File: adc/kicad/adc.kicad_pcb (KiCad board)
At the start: 2 copper layers, 34.4 x 27.5 mm, 70 parts, among them J1 Conn_01x05_Pin, J2 Conn_01x06_Pin, J3 Conn_01x05_Pin, J4 Conn_01x03_Pin, U1 ESD5344D-TP, U2 ESD5344D-TP, U3 ADS1261B, U4 ESD5344D-TP, U5 TPS7A2050PDBVR, U6 TPS61252DSG, U7 XC6206P332MR

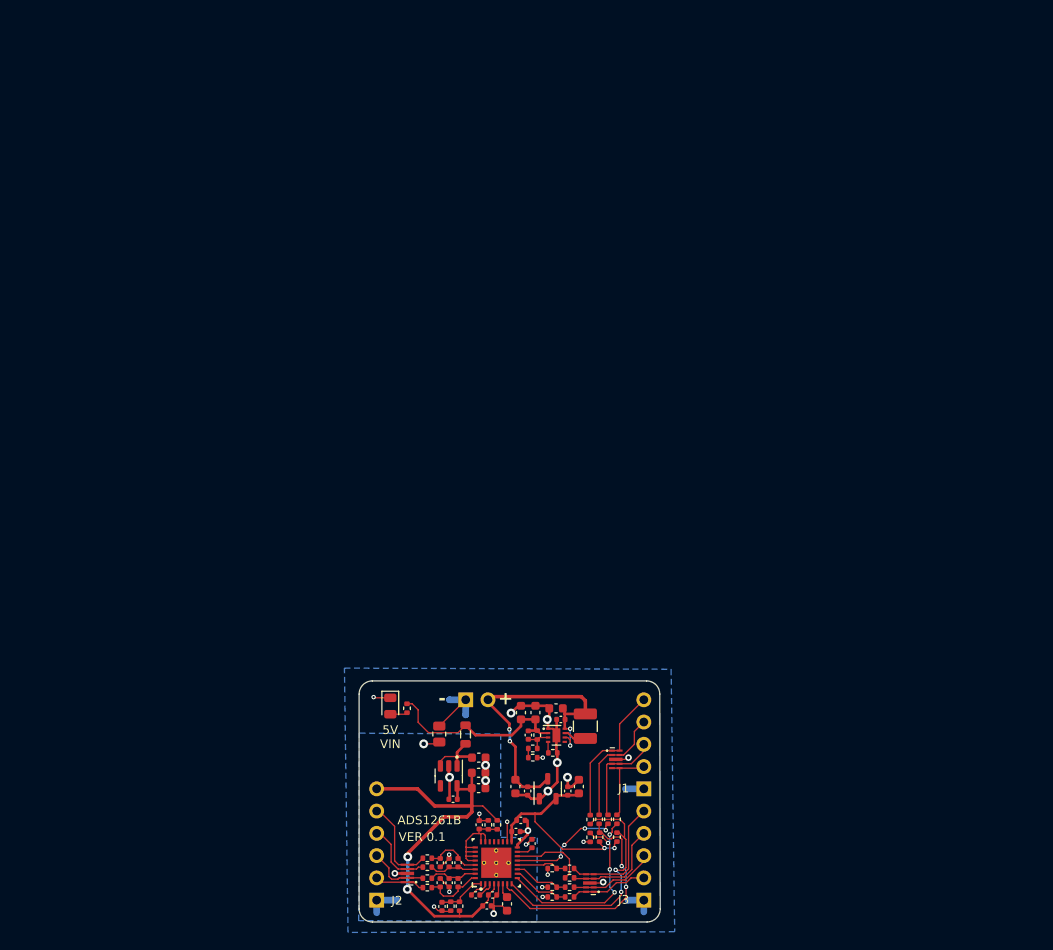
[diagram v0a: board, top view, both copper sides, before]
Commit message: Progressing on the ADC layout.
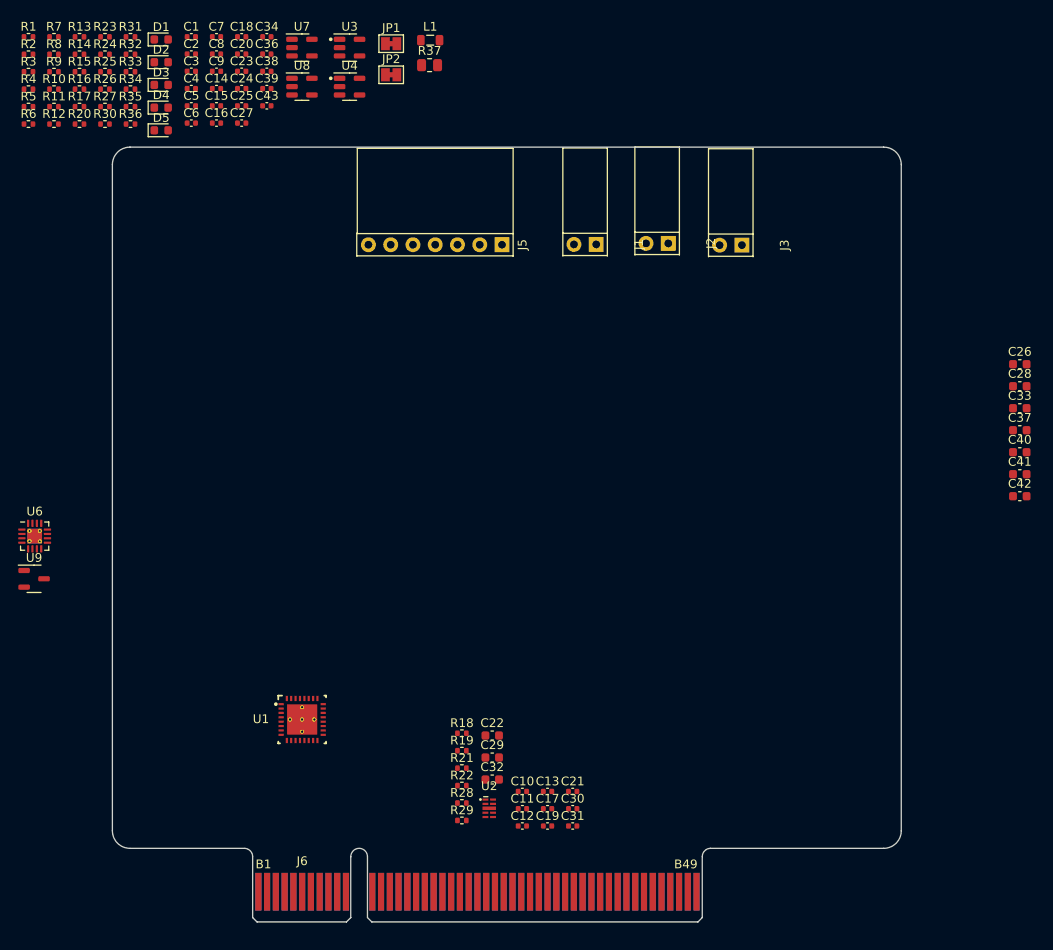
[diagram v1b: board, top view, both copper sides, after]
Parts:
- removed FB1: Ferrite Bead, Inductor_SMD:L_0805_2012Metric
- removed J4: Conn_01x03_Pin, adc:PinHeader_1x02_P2.54mm_Vertical
- removed U5: TPS7A2050PDBVR, adc:SOT-23-5
- added C29: 10u, Capacitor_SMD:C_0603_1608Metric, F.Cu at (15.2, -18.8)
- added C30: 100n, Capacitor_SMD:C_0402_1005Metric, F.Cu at (24.4, -12.9)
- added C31: 100n, Capacitor_SMD:C_0402_1005Metric, F.Cu at (24.4, -10.9)
- added C32: 10u, Capacitor_SMD:C_0603_1608Metric, F.Cu at (15.2, -16.2)
- added C33: 10u, Capacitor_SMD:C_0603_1608Metric, F.Cu at (75.4, -58.6)
- added C34: 100n, Capacitor_SMD:C_0402_1005Metric, F.Cu at (-10.5, -101.0)
- added C36: 100n, Capacitor_SMD:C_0402_1005Metric, F.Cu at (-10.5, -99.0)
- added C37: 10u, Capacitor_SMD:C_0603_1608Metric, F.Cu at (75.4, -56.1)
- added C38: 100n, Capacitor_SMD:C_0402_1005Metric, F.Cu at (-10.5, -97.0)
- added C39: 100n, Capacitor_SMD:C_0402_1005Metric, F.Cu at (-10.5, -95.1)
- added C40: 10u, Capacitor_SMD:C_0603_1608Metric, F.Cu at (75.4, -53.6)
- added C41: 10u, Capacitor_SMD:C_0603_1608Metric, F.Cu at (75.4, -51.1)
- added C42: 10u, Capacitor_SMD:C_0603_1608Metric, F.Cu at (75.4, -48.6)
- added C43: 100n, Capacitor_SMD:C_0402_1005Metric, F.Cu at (-10.5, -93.1)
- added D2: RED, LED_SMD:LED_0603_1608Metric, F.Cu at (-22.6, -98.1)
- added D3: RED, LED_SMD:LED_0603_1608Metric, F.Cu at (-22.6, -95.5)
- added D4: RED, LED_SMD:LED_0603_1608Metric, F.Cu at (-22.6, -92.9)
- added D5: RED, LED_SMD:LED_0603_1608Metric, F.Cu at (-22.6, -90.3)
- added J2: Conn_01x02_Pin, adc:connector_2pins_horizontal, F.Cu at (34.0, -77.4)
- added J6: pcie_98, common:PCIE_98_CARD, F.Cu at (0.00, 0.00)
- added JP1: SolderJumper_2_Bridged, Jumper:SolderJumper-2_P1.3mm_Bridged_Pad1.0x1.5mm, F.Cu at (3.66, -100.2)
- added JP2: SolderJumper_2_Bridged, Jumper:SolderJumper-2_P1.3mm_Bridged_Pad1.0x1.5mm, F.Cu at (3.66, -96.7)
- added R29: 51K, Resistor_SMD:R_0402_1005Metric, F.Cu at (11.7, -11.6)
- added R30: 1K 0.1% 10ppm, Resistor_SMD:R_0402_1005Metric, F.Cu at (-29.0, -91.0)
- added R31: 360K 0.1%, Resistor_SMD:R_0402_1005Metric, F.Cu at (-26.1, -101.0)
- added R32: 100K 0.1%, Resistor_SMD:R_0402_1005Metric, F.Cu at (-26.1, -99.0)
- added R33: 464K 0.1%, Resistor_SMD:R_0402_1005Metric, F.Cu at (-26.1, -97.0)
- added R34: 1K, Resistor_SMD:R_0402_1005Metric, F.Cu at (-26.1, -95.0)
- added R35: 1K 0.1% 10ppm, Resistor_SMD:R_0402_1005Metric, F.Cu at (-26.1, -93.0)
- added R36: 1K 0.1% 10ppm, Resistor_SMD:R_0402_1005Metric, F.Cu at (-26.1, -91.0)
- added R37: 0R, Resistor_SMD:R_0805_2012Metric, F.Cu at (8.04, -97.8)
- added U8: ADP7182AUJZ-2.5, Package_TO_SOT_SMD:TSOT-23-5, F.Cu at (-6.52, -95.3)
- added U9: XC6206P332MR, Package_TO_SOT_SMD:SOT-23-3, F.Cu at (-37.1, -39.1)
- C1, C5: value 1u -> 2u2
- C10: value 1n -> 1u
- C11: value 10n -> 1u
- C12: value 4n7 -> 100n
- C13, C8: value 1n -> 100n
- C14: value 1u -> 22n
- C15, C19: value 10u -> 220n; footprint Capacitor_SMD:C_0603_1608Metric -> Capacitor_SMD:C_0402_1005Metric
- C16: value 100pf -> 22n
- C17: value 10u -> 4n7; footprint Capacitor_SMD:C_0603_1608Metric -> Capacitor_SMD:C_0402_1005Metric
- C18: value 10u -> 22n; footprint Capacitor_SMD:C_0603_1608Metric -> Capacitor_SMD:C_0402_1005Metric
- C2, C9: value 1u -> 100n
- C20: value 100n -> 22n
- C21: value 10u -> 1u; footprint Capacitor_SMD:C_0603_1608Metric -> Capacitor_SMD:C_0402_1005Metric
- C22, C26: value 100n -> 10u; footprint Capacitor_SMD:C_0402_1005Metric -> Capacitor_SMD:C_0603_1608Metric
- C23, C24, C25: value 10u -> 100n; footprint Capacitor_SMD:C_0603_1608Metric -> Capacitor_SMD:C_0402_1005Metric
- C6: value 1n -> 2u2
- C7: value 10n -> 100n
- D1: footprint LED_SMD:LED_0805_2012Metric -> LED_SMD:LED_0603_1608Metric
- J1, J3: value Conn_01x05_Pin -> Conn_01x02_Pin; footprint adc:PinHeader_1x05_P2.54mm_Vertical -> adc:connector_2pins_horizontal
- J5: renamed from J2; value Conn_01x06_Pin -> Conn_01x07_Pin; footprint adc:PinHeader_1x06_P2.54mm_Vertical -> adc:connector_7pins_horizontal
- L1: value 1uH -> 2u2H; footprint Inductor_SMD:L_1210_3225Metric -> Inductor_SMD:L_0805_2012Metric
- R1, R13, R2, R7: value 51K -> 1K 0.1% 10ppm
- R10: value 100R -> 470R
- R11, R9: value 47R -> 470R
- R12, R17, R8: value 47R -> 1K 0.1% 10ppm
- R14, R3: value 100R -> 1K 0.1% 10ppm
- R15, R16: value 47R -> 51K
- R19: value 100R -> 47R
- R20: value 51K -> 1K
- R21, R22: value 51K -> 47R
- R23: value 510K -> 5K1
- R25: value 120K -> 5K1
- R26: value 20K -> 5K1
- R27: value 0R -> 5K1; footprint Resistor_SMD:R_0805_2012Metric -> Resistor_SMD:R_0402_1005Metric
- R28: value 22K -> 51K
- R4, R5, R6: value 51K -> 470R
- U1: value ESD5344D-TP -> ADS1261B; footprint common:Diodes_UDFN-10_1.0x2.5mm_P0.5mm -> adc:RHB0032E
- U3: value ADS1261B -> TPS7A2050PDBVR; footprint adc:RHB0032E -> adc:SOT-23-5
- U4: value ESD5344D-TP -> TPS7A2025PDBVR; footprint common:Diodes_UDFN-10_1.0x2.5mm_P0.5mm -> adc:SOT-23-5
- U6: value TPS61252DSG -> TPS65135; footprint adc:WSON-8-1EP_2x2mm_P0.5mm_EP0.9x1.6mm -> Package_DFN_QFN:WQFN-16-1EP_3x3mm_P0.5mm_EP1.68x1.68mm_ThermalVias
- U7: value XC6206P332MR -> ADP7182AUJZ-5.0; footprint Package_TO_SOT_SMD:SOT-23-3 -> Package_TO_SOT_SMD:TSOT-23-5
- moved R1 110.7 mm to (-37.7, -101.0), turned to 0 degrees
- moved R2 108.5 mm to (-37.7, -99.0), turned to 0 degrees
- moved R13 108.3 mm to (-31.9, -101.0), turned to 0 degrees
- moved R5 107.0 mm to (-37.7, -93.0), turned to 0 degrees
- moved R15 106.7 mm to (-31.9, -97.0), turned to 0 degrees
- moved R8 106.6 mm to (-34.8, -99.0), turned to 0 degrees
- moved R16 105.9 mm to (-31.9, -95.0), turned to 0 degrees
- moved R9 105.6 mm to (-34.8, -97.0), turned to 0 degrees
- moved R17 105.1 mm to (-31.9, -93.0), turned to 0 degrees
- moved C1 104.7 mm to (-19.1, -101.0), turned to 0 degrees
- moved R6 104.2 mm to (-37.7, -91.0), turned to 0 degrees
- moved R20 103.4 mm to (-31.9, -91.0)
- moved R11 103.0 mm to (-34.8, -93.0), turned to 0 degrees
- moved R7 102.7 mm to (-34.8, -101.0), turned to 0 degrees
- moved R12 102.1 mm to (-34.8, -91.0), turned to 0 degrees
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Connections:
- C1 pad 1: GNDA -> /AIN6
- C1 pad 2: +5VA -> /AIN7
- C10 pad 1: /AIN1 -> GNDA
- C10 pad 2: GNDA -> /+2V5A
- C11 pad 1: /AIN1 -> /+3V3D
- C11 pad 2: /AIN0 -> GNDD
- C12 pad 1: Net-(U3-CAPN) -> GNDA
- C12 pad 2: Net-(U3-CAPP) -> /+2V5A
- C13 pad 1: GNDA -> /+3V3D
- C13 pad 2: /AIN0 -> GNDD
- C14 pad 1: Net-(U3-BYPASS) -> /AIN2
- C15 pad 1: Net-(U3-REFOUT) -> /AIN0
- C15 pad 2: GNDA -> /AIN1
- C16 pad 1: Net-(U6-FB) -> GNDA
- C16 pad 2: Net-(U6-VOUT) -> /AIN1
- C17 pad 1: GNDD -> Net-(U1-CAPN)
- C17 pad 2: Net-(J4-Pin_2) -> Net-(U1-CAPP)
- C18 pad 1: GNDD -> /AIN0
- C18 pad 2: Net-(U6-VOUT) -> GNDA
- C19 pad 1: GNDD -> /AIN2
- C19 pad 2: Net-(U6-VOUT) -> /AIN3
- C2 pad 1: +3V3 -> GNDA
- C2 pad 2: GNDD -> /AIN6
- C20 pad 1: GNDD -> GNDA
- C20 pad 2: Net-(J4-Pin_2) -> /AIN3
- C21 pad 1: GNDA -> Net-(U1-BYPASS)
- C21 pad 2: Net-(U5-EN) -> GNDA
- C22 pad 1: GNDA -> Net-(U1-REFOUT)
- C22 pad 2: +5VA -> GNDA
- C23 pad 2: +5VA -> /+5V7
- C24 pad 2: +5VA -> /+5VA
- C25 pad 1: GNDD -> GNDA
- C25 pad 2: Net-(J4-Pin_2) -> /+5VA
- C26 pad 1: GNDD -> GNDA
- C26 pad 2: Net-(J4-Pin_2) -> /+5VA
- C27 pad 1: GNDD -> GNDA
- C27 pad 2: +3V3 -> /+2V5A
- C28 pad 1: GNDD -> GNDA
- C28 pad 2: +3V3 -> /+2V5A
- C3 pad 2: +5VA -> /AIN4
- C4 pad 1: +3V3 -> /AIN7
- C4 pad 2: GNDD -> GNDA
- C5 pad 1: GNDA -> /AIN8
- C5 pad 2: Net-(U3-AINCOM) -> /AIN9
- C6 pad 1: /AIN3 -> /AIN4
- C6 pad 2: GNDA -> /AIN5
- C7 pad 1: /AIN3 -> GNDA
- C7 pad 2: /AIN2 -> /AIN8
- C8 pad 1: GNDA -> /AIN9
- C8 pad 2: /AIN2 -> GNDA
- C9 pad 1: GNDA -> /AIN5
- C9 pad 2: Net-(U3-AIN4) -> GNDA
- D1 pad 1: GNDD -> GNDA
- J1 pad 1: GNDD -> Net-(J1-Pin_1)
- J3 pad 1: GNDD -> Net-(J3-Pin_1)
- J5 pad 1: GNDA -> /-5VA
- J5 pad 2: Net-(J2-Pin_2) -> Net-(J5-Pin_2)
- J5 pad 3: Net-(J2-Pin_3) -> Net-(J5-Pin_3)
- J5 pad 4: Net-(J2-Pin_4) -> GNDA
- J5 pad 5: Net-(J2-Pin_5) -> Net-(J5-Pin_5)
- J5 pad 6: +5VA -> Net-(J5-Pin_6)
- L1 pad 1: Net-(J4-Pin_2) -> Net-(L1-Pad1)
- L1 pad 2: Net-(U6-SW) -> Net-(L1-Pad2)
- R1 pad 1: Net-(U3-AINCOM) -> Net-(J1-Pin_2)
- R1 pad 2: +5VA -> /+2V5A
- R10 pad 1: Net-(J2-Pin_4) -> Net-(J2-Pin_2)
- R10 pad 2: /AIN2 -> /AIN8
- R11 pad 1: Net-(J1-Pin_3) -> Net-(J2-Pin_1)
- R11 pad 2: Net-(U3-DRDY_N) -> /AIN9
- R12 pad 1: Net-(J1-Pin_2) -> /-2V5A
- R12 pad 2: Net-(U3-START) -> Net-(J3-Pin_1)
- R13 pad 1: GNDD -> /AIN0
- R13 pad 2: Net-(U3-START) -> Net-(R13-Pad2)
- R14 pad 1: Net-(J2-Pin_3) -> Net-(R14-Pad1)
- R14 pad 2: /AIN1 -> /AIN0
- R15 pad 1: Net-(J3-Pin_5) -> Net-(U1-MISO)
- R15 pad 2: Net-(U3-DIN) -> /+3V3D
- R16 pad 1: Net-(J3-Pin_4) -> Net-(U1-CS_N)
- R16 pad 2: Net-(U3-DOUT_DRDY_N) -> /+3V3D
- R17 pad 1: Net-(J3-Pin_3) -> Net-(R13-Pad2)
- R17 pad 2: Net-(U3-SCLK) -> Net-(J5-Pin_6)
- R18 pad 1: Net-(J3-Pin_2) -> /PA7
- R18 pad 2: Net-(U3-CS_N) -> Net-(U1-MOSI)
- R19 pad 1: Net-(J2-Pin_2) -> /PA6
- R19 pad 2: /AIN0 -> Net-(U1-MISO)
- R2 pad 1: GNDA -> /-2V5A
- R2 pad 2: Net-(U3-AINCOM) -> Net-(J1-Pin_1)
- R20 pad 1: GNDD -> Net-(J5-Pin_3)
- R20 pad 2: Net-(U3-CS_N) -> /AIN3
- R21 pad 1: GNDD -> /PA5
- R21 pad 2: Net-(U3-SCLK) -> Net-(U1-SCLK)
- R22 pad 1: GNDD -> /PB14
- R22 pad 2: Net-(U3-DIN) -> Net-(U1-CS_N)
- R23 pad 1: Net-(U6-VOUT) -> /+5VA
- R23 pad 2: Net-(U6-FB) -> Net-(D1-A)
- R24 pad 1: Net-(U6-VOUT) -> /-5VA
- R24 pad 2: Net-(D1-A) -> Net-(D2-A)
- R25 pad 1: Net-(R25-Pad1) -> /+2V5A
- R25 pad 2: Net-(U6-FB) -> Net-(D3-A)
- R26 pad 1: Net-(U6-ILIM) -> /-2V5A
- R26 pad 2: GNDD -> Net-(D4-A)
- R27 pad 1: GNDD -> /+3V3D
- R27 pad 2: GNDA -> Net-(D5-A)
- R28 pad 2: Net-(R25-Pad1) -> Net-(U1-MOSI)
- R3 pad 1: Net-(J2-Pin_5) -> Net-(J3-Pin_2)
- R3 pad 2: /AIN3 -> /+2V5A
- R4 pad 1: Net-(U3-AIN4) -> Net-(J1-Pin_2)
- R4 pad 2: +5VA -> /AIN6
- R5 pad 1: Net-(U3-RESET_N) -> Net-(J1-Pin_1)
- R5 pad 2: +3V3 -> /AIN7
- R6 pad 1: Net-(U3-PWDN_N) -> Net-(J3-Pin_2)
- R6 pad 2: +3V3 -> /AIN4
- R7 pad 1: GNDA -> Net-(J2-Pin_2)
- R7 pad 2: Net-(U3-AIN4) -> /+2V5A
- R8 pad 1: Net-(J1-Pin_5) -> /-2V5A
- R8 pad 2: Net-(U3-RESET_N) -> Net-(J2-Pin_1)
- R9 pad 1: Net-(J1-Pin_4) -> Net-(J3-Pin_1)
- R9 pad 2: Net-(U3-PWDN_N) -> /AIN5
- U1 pad 1: Net-(J1-Pin_5) -> GNDA
- U1 pad 2: Net-(J1-Pin_4) -> Net-(U1-CAPP)
- U1 pad 3: GNDD -> Net-(U1-CAPN)
- U1 pad 4: Net-(J1-Pin_3) -> /+2V5A
- U1 pad 5: Net-(J1-Pin_2) -> /-2V5A
- U2 pad 1: Net-(J2-Pin_2) -> /PB14
- U2 pad 2: Net-(J2-Pin_3) -> /PA5
- U2 pad 3: GNDA -> GNDD
- U2 pad 4: Net-(J2-Pin_4) -> /PA6
- U2 pad 5: Net-(J2-Pin_5) -> /PA7
- U3 pad 1: Net-(U3-AINCOM) -> /+5V7
- U3 pad 2: Net-(U3-CAPP) -> GNDA
- U3 pad 3: Net-(U3-CAPN) -> /+5V7
- U3 pad 4: +5VA -> unconnected-(U3-NC-Pad4)
- U3 pad 5: GNDA -> /+5VA
- U4 pad 1: Net-(J3-Pin_2) -> /+5VA
- U4 pad 2: Net-(J3-Pin_3) -> GNDA
- U4 pad 3: GNDD -> /+5VA
- U4 pad 4: Net-(J3-Pin_4) -> unconnected-(U4-NC-Pad4)
- U4 pad 5: Net-(J3-Pin_5) -> /+2V5A
- U6 pad 1: GNDD -> +5VD
- U6 pad 2: Net-(U6-VOUT) -> /-5V7
- U6 pad 3: Net-(U6-FB) -> /-5V7
- U6 pad 4: Net-(U6-ILIM) -> Net-(U6-VAUX)
- U6 pad 5: unconnected-(U6-PG-Pad5) -> GNDA
- U6 pad 6: Net-(J4-Pin_2) -> Net-(U6-FBG)
- U6 pad 7: Net-(U6-SW) -> Net-(U6-FB)
- U6 pad 8: Net-(J4-Pin_2) -> +5VD
- U6 pad 9: GNDD -> /+5V7
- U7 pad 1: GNDD -> GNDA
- U7 pad 2: +3V3 -> /-5V7
- U7 pad 3: Net-(J4-Pin_2) -> /-5V7
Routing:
- net GNDD: track 53.4 -> 0.00 mm, vias 15 -> 0
- net +5VA: track 50.2 -> 0.00 mm, vias 2 -> 0
- net Net-(J4-Pin_2): track 37.6 -> 0.00 mm, vias 4 -> 0
- net Net-(U3-RESET_N): track 29.0 -> 0.00 mm, vias 2 -> 0
- net Net-(U3-PWDN_N): track 26.4 -> 0.00 mm, vias 2 -> 0
- net GNDA: track 24.8 -> 0.00 mm, vias 11 -> 0
- net +3V3: track 24.1 -> 0.00 mm, vias 2 -> 0
- net Net-(U3-START): track 23.9 -> 0.00 mm, vias 4 -> 0
- net Net-(U6-VOUT): track 22.6 -> 0.00 mm
- net Net-(J1-Pin_5): track 16.8 -> 0.00 mm
- net Net-(J1-Pin_4): track 14.1 -> 0.00 mm
- net Net-(J3-Pin_5): track 14.0 -> 0.00 mm
- net Net-(U3-AIN4): track 13.2 -> 0.00 mm
- net Net-(U3-DRDY_N): track 13.1 -> 0.00 mm, vias 4 -> 0
- net Net-(J3-Pin_4): track 11.8 -> 0.00 mm
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- removed copper zone on B.Cu, net GNDA
- removed copper zone on B.Cu, net GNDD
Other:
- board size 34.4 x 27.5 mm -> 90 x 88.4 mm
- board text removed: "+"
- board text removed: "-"
- board text removed: "5V VIN"
- board text removed: "ADS1261B"
- board text removed: "VER 0.1"

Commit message: More progress with the ADC layout.
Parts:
- moved C37 97.2 mm to (-20.2, -38.4), turned to 90 degrees
- moved C40 96.1 mm to (-20.3, -44.8), turned to 90 degrees
- moved R10 93.6 mm to (56.1, -72.8)
- moved R11 93.6 mm to (56.1, -70.8)
- moved R7 91.8 mm to (52.9, -74.0)
- moved R8 91.8 mm to (52.9, -72.0)
- moved C41 91.1 mm to (-12.7, -27.6)
- moved C26 89.1 mm to (-10.1, -38.4), turned to 90 degrees
- moved C42 88.8 mm to (-11.5, -30.0), turned to 90 degrees
- moved C33 87.2 mm to (-5.75, -26.5), turned to 90 degrees
- moved C28 86.8 mm to (-10.2, -46.3), turned to 90 degrees
- moved R15 86.0 mm to (33.4, -41.1)
- moved R2 85.7 mm to (43.5, -71.8), turned to 90 degrees
- moved R5 85.7 mm to (44.5, -69.2)
- moved R16 85.1 mm to (32.4, -39.3)
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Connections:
- U2 pad 2: /PA5 -> /PA6
- U2 pad 4: /PA6 -> /PA7
- U2 pad 5: /PA7 -> /PA5
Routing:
- net GNDA: track 0.00 -> 98.4 mm, vias 0 -> 15
- net +5VD: track 0.00 -> 94.7 mm
- net /-5VA: track 0.00 -> 89.6 mm
- net GNDD: track 0.00 -> 88.5 mm, vias 0 -> 3
- net /+5VA: track 0.00 -> 68.6 mm
- net /-2V5A: track 0.00 -> 25.5 mm, vias 0 -> 2
- net /-5V7: track 0.00 -> 20.5 mm, vias 0 -> 2
- net /PB14: track 0.00 -> 19.7 mm
- net /PA7: track 0.00 -> 17.3 mm, vias 0 -> 1
- net /PA5: track 0.00 -> 17.1 mm
- net /PA6: track 0.00 -> 14.3 mm
- net (no net): track 0.00 -> 14.1 mm
- net /+2V5A: track 0.00 -> 13.5 mm
- net /AIN1: track 0.00 -> 12.5 mm, vias 0 -> 2
- net /+5V7: track 0.00 -> 8.38 mm
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
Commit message: Initial topological routing of the ADC board completed.
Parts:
- added C35: 1u, Capacitor_SMD:C_0402_1005Metric, F.Cu at (16.6, -49.3)
- added C44: 100n, Capacitor_SMD:C_0402_1005Metric, F.Cu at (18.1, -49.7)
- added C45: 1u, Capacitor_SMD:C_0402_1005Metric, F.Cu at (23.0, -74.4)
- added C46: 1u, Capacitor_SMD:C_0402_1005Metric, F.Cu at (5.05, -74.2)
- added C47: 10u, Capacitor_SMD:C_0603_1608Metric, F.Cu at (2.04, -39.7)
- added C48: 10u, Capacitor_SMD:C_0603_1608Metric, F.Cu at (2.04, -37.2)
- moved R22 15.9 mm to (19.7, -42.6)
- moved R15 15.8 mm to (18.5, -36.1), turned to 180 degrees
- moved R16 14.6 mm to (18.6, -34.6), turned to 180 degrees
- moved R29 14.6 mm to (22.8, -30.6), turned to 180 degrees
- moved R18 11.8 mm to (22.7, -42.6)
- moved R28 11.3 mm to (22.8, -32.4), turned to 180 degrees
- moved R21 9.77 mm to (21.4, -42.6)
- moved R19 9.65 mm to (24.0, -42.5)
- moved R37 8.76 mm to (-2.01, -33.2), turned to -90 degrees
- moved C1 8.71 mm to (42.8, -72.9)
- moved C6 7.80 mm to (32.7, -72.5)
- moved C9 7.32 mm to (34.5, -72.0), turned to -90 degrees
- moved C8 6.38 mm to (55.3, -72.9), turned to -90 degrees
- moved C2 5.80 mm to (41.2, -72.6), turned to 90 degrees
- moved R4 5.72 mm to (41.5, -74.6), turned to -90 degrees
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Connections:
- C33 pad 2: GNDA -> GNDD
- C41 pad 1: GNDA -> GNDD
- C42 pad 2: GNDA -> GNDD
- C43 pad 2: GNDA -> GNDD
- R15 pad 1: Net-(U1-MISO) -> /PA6
- R16 pad 1: Net-(U1-CS_N) -> /PB14
- R28 pad 2: Net-(U1-MOSI) -> /PA7
- R29 pad 2: Net-(U1-SCLK) -> /PA5
- U6 pad 11: GNDA -> GNDD
- U6 pad 12: GNDA -> GNDD
- U6 pad 17: GNDA -> GNDD
- U6 pad 5: GNDA -> GNDD
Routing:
- net /-2V5A: track 25.5 -> 166.1 mm, vias 2 -> 8
- net /+2V5A: track 13.5 -> 139.2 mm, vias 0 -> 2
- net /AIN9: track 0.00 -> 41.2 mm
- net /AIN8: track 0.00 -> 40.3 mm
- net GNDA: track 98.4 -> 61.0 mm, vias 15 -> 16
- net /PA7: track 17.3 -> 52.7 mm, vias 1 -> 3
- net /PA6: track 14.3 -> 48.3 mm, vias 0 -> 3
- net GNDD: track 88.5 -> 120.0 mm, vias 3 -> 10
- net /PA5: track 17.1 -> 47.5 mm
- net /AIN7: track 0.00 -> 30.1 mm
- net /AIN6: track 0.00 -> 29.9 mm
- net /PB14: track 19.7 -> 48.3 mm
- net /+3V3D: track 7.79 -> 36.2 mm, vias 0 -> 2
- net /AIN4: track 0.00 -> 26.2 mm
- net /AIN5: track 0.00 -> 26.1 mm
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
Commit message: ADC layout is feature complete.
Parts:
- R10, R11, R4, R5, R6, R9: value 470R -> 1K
- moved C5 36.9 mm to (17.6, -66.2), turned to -90 degrees
- moved C1 27.2 mm to (16.1, -67.7), turned to -90 degrees
- moved C48 20.2 mm to (-13.6, -50.1)
- moved C12 19.0 mm to (6.12, -65.6), turned to -90 degrees
- moved C6 18.4 mm to (14.7, -69.2), turned to -90 degrees
- moved C10 18.3 mm to (5.11, -65.6)
- moved C11 18.0 mm to (16.1, -62.8)
- moved C13 18.0 mm to (15.1, -62.8)
- moved C35 17.9 mm to (5.84, -63.6)
- moved C44 17.9 mm to (6.86, -63.6), turned to 90 degrees
- moved C21 17.8 mm to (13.1, -60.8), turned to 0 degrees
- moved U1 17.8 mm to (11.2, -64.6)
- moved C17 17.7 mm to (7.24, -66.0)
- moved C22 17.2 mm to (7.34, -60.8)
- moved R29 16.8 mm to (20.0, -47.1)
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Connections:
- D5 pad 1: GNDA -> GNDD
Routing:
- net /+3V3D: track 36.2 -> 142.6 mm, vias 2 -> 4
- net /+5V7: track 17.6 -> 39.6 mm
- net /-2V5A: track 166.1 -> 146.2 mm
- net /AIN0: track 25.1 -> 7.40 mm
- net /AIN1: track 29.9 -> 12.4 mm
- net /AIN2: track 25.5 -> 8.44 mm
- net /AIN3: track 25.3 -> 8.50 mm
- net /+2V5A: track 139.2 -> 122.9 mm, vias 2 -> 3
- net /PA5: track 47.5 -> 62.3 mm, vias 0 -> 2
- net /-5V7: track 20.5 -> 34.1 mm
- net /PA6: track 48.3 -> 60.2 mm, vias 3 -> 2
- net /PB14: track 48.3 -> 58.1 mm
- net /PA7: track 52.7 -> 60.6 mm
- net Net-(D5-A): track 0.00 -> 6.19 mm
- net Net-(D4-A): track 0.00 -> 6.19 mm
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- added copper zone on B.Cu, net GNDA
- added copper zone on B.Cu, net GNDD
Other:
- board text added: "+2V5A"
- board text added: "+3V3"
- board text added: "+5VA"
- board text added: "-2V5A"
- board text added: "ADC VER 0.1"
- board text added: "LOAD CELL"
- board text added: "THERM1"
- board text added: "THERM2"
- board text added: "THERM3"

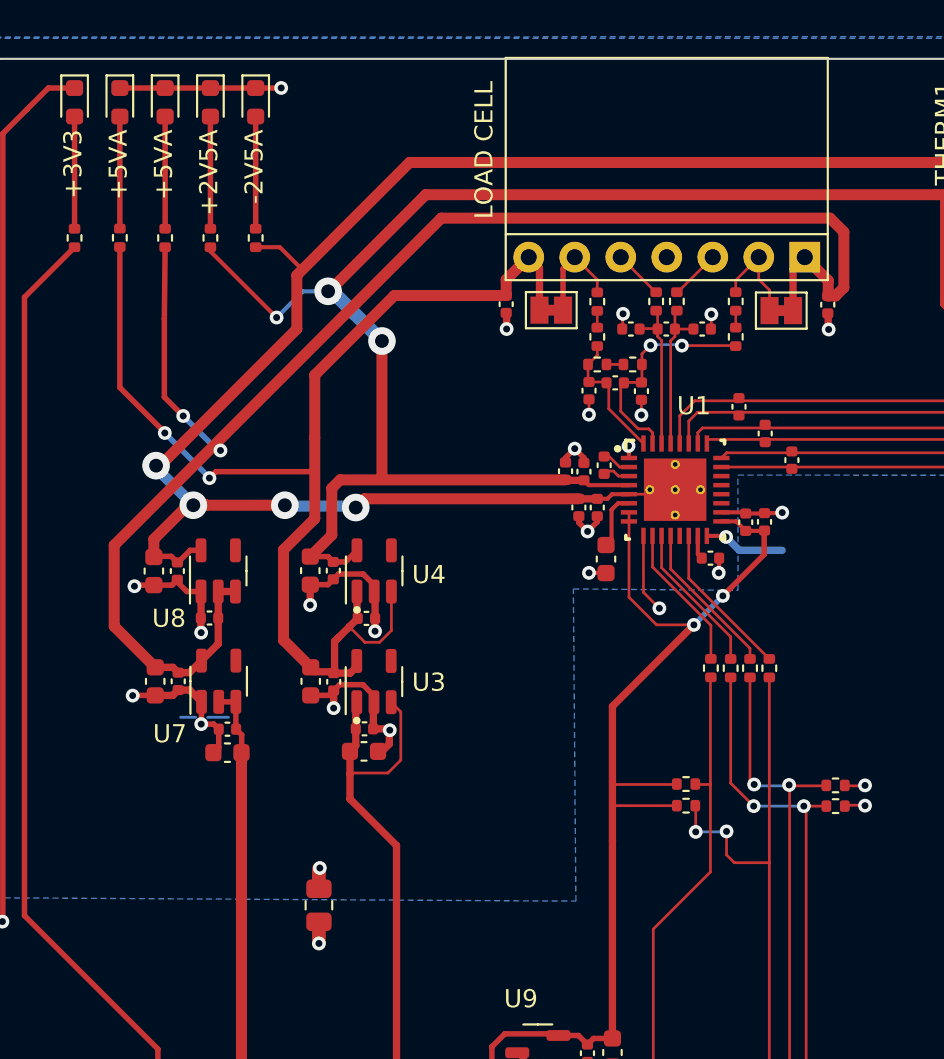
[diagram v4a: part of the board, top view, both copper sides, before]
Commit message: Tweaked the ADC layout.
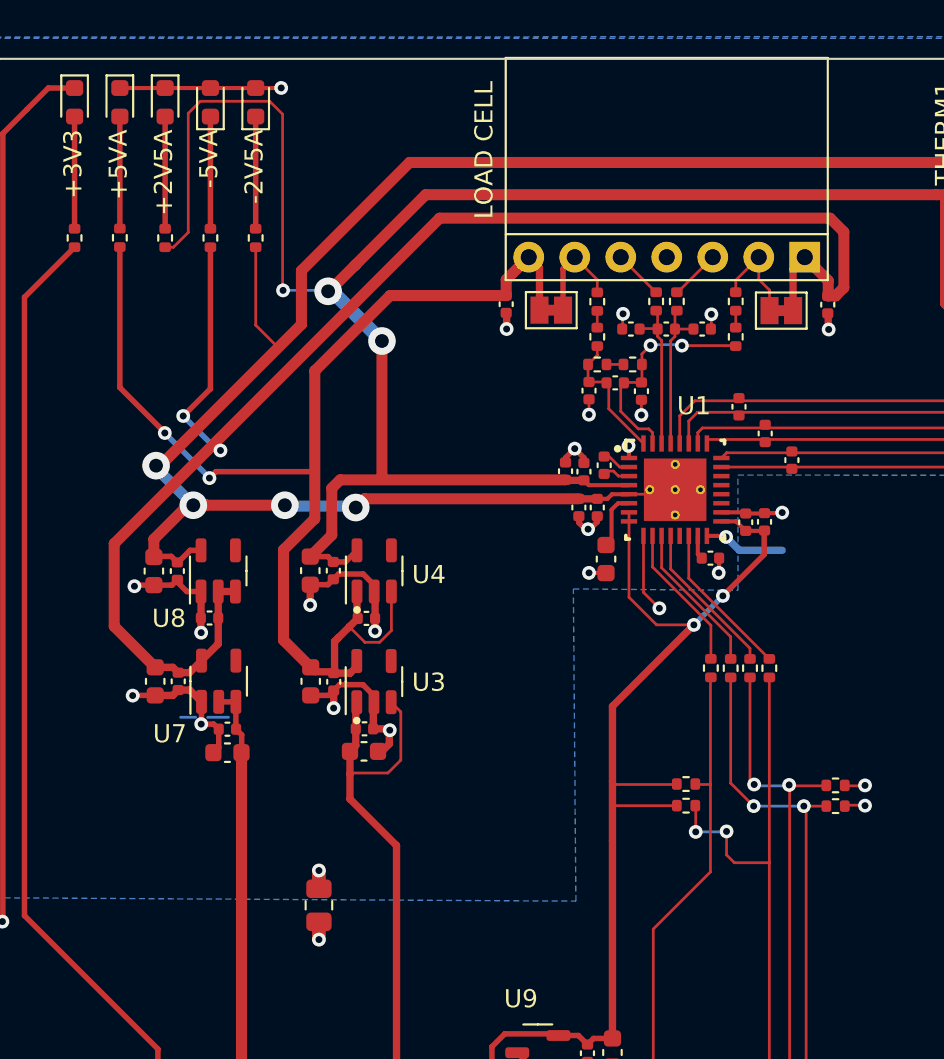
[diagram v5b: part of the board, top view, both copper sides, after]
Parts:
- U1: value ADS1261B -> ADS1261BIRHBT
- U4: value TPS7A2025PDBVR -> TPS7A2025PDBVRr
- moved D2 2.50 mm to (-14.5, -86.0), turned to 90 degrees
- moved D3 2.50 mm to (-17.0, -86.0)
- moved R24 2.50 mm to (-14.5, -78.5)
- moved R25 2.50 mm to (-17.0, -78.5)
- turned D4 to 90 degrees
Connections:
- D2 pad 1: GNDA -> Net-(D2-K)
- D2 pad 2: Net-(D2-A) -> GNDA
- D4 pad 1: GNDA -> Net-(D4-K)
- D4 pad 2: Net-(D4-A) -> GNDA
- R24 pad 2: Net-(D2-A) -> Net-(D2-K)
- R26 pad 2: Net-(D4-A) -> Net-(D4-K)
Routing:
- net /+2V5A: track 122.9 -> 140.3 mm
- net Net-(D4-K): track 0.00 -> 6.19 mm
- net Net-(D4-A): track 6.19 -> 0.00 mm
- net Net-(D2-K): track 0.00 -> 6.19 mm
- net Net-(D2-A): track 6.19 -> 0.00 mm
- net /-2V5A: track 146.2 -> 149.1 mm
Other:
- board text added: "-5VA"
